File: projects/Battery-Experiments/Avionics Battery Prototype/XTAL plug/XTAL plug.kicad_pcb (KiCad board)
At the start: 2 copper layers, 19.1 x 7.6 mm, 2 parts, among them J1 Conn_01x02, X1 Crystal

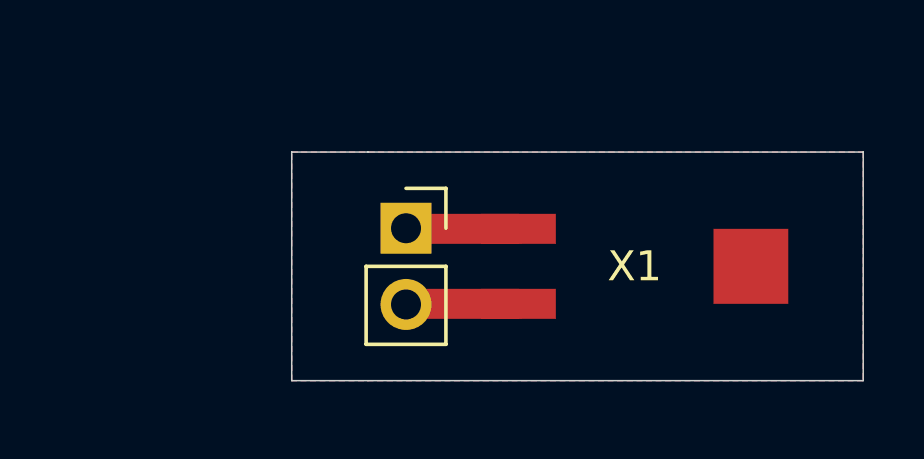
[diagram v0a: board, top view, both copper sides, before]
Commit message: AVB Rev C and XTAL Plug Final
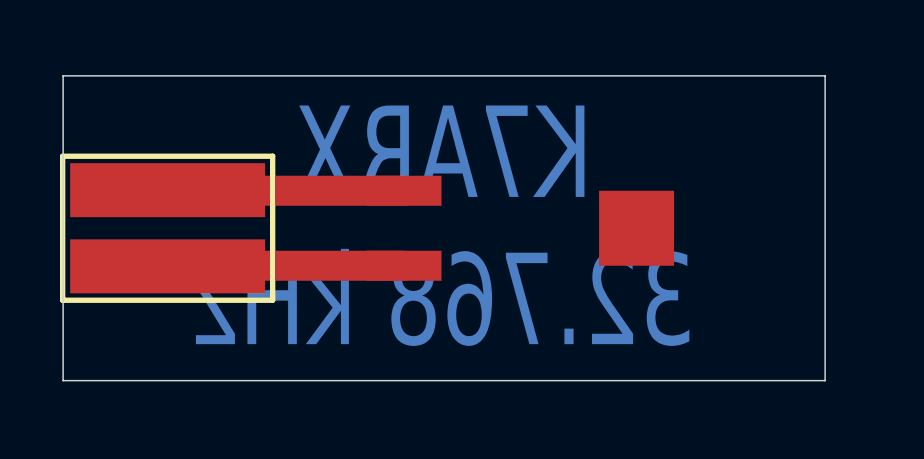
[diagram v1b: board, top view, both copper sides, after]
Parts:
- J1: footprint Connector_PinSocket_2.54mm:PinSocket_1x02_P2.54mm_Vertical -> k7arx:PreciDip 8MM-11 2-pin SMD
- moved J1 4.44 mm to (146.7, 127.0), turned to 270 degrees
- moved X1 4.02 mm to (154.9, 127.0)
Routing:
- net Net-(J1-Pad2): track 3.75 -> 7.86 mm
- net Net-(J1-Pad1): track 3.75 -> 7.86 mm
- removed copper zone on B.Cu, net GND
- removed copper zone on F.Cu, net GND
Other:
- board size 19.1 x 7.6 mm -> 25.4 x 10.2 mm
- board text added: "K7ARX 32.768 kHz"
- board text removed: "K7ARX Crystal Frequency"
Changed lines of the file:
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@@
-(kicad_pcb (version 20171130) (host pcbnew 5.1.9)
+(kicad_pcb (version 20171130) (host pcbnew "(5.1.9)-1")
   (general
     (thickness 1.6)
-    (drawings 8)
-    (tracks 4)
+    (drawings 5)
+    (tracks 2)
     (zones 0)
     (modules 2)
@@
   )
   (layers
-    (0 F.Cu signal hide)
+    (0 F.Cu signal)
     (31 B.Cu signal)
     (32 B.Adhes user)
     (33 F.Adhes user)
     (34 B.Paste user)
-    (35 F.Paste user hide)
+    (35 F.Paste user)
     (36 B.SilkS user)
     (37 F.SilkS user)
     (38 B.Mask user)
-    (39 F.Mask user hide)
+    (39 F.Mask user)
     (40 Dwgs.User user)
     (41 Cmts.User user)
@@
     (pad_to_mask_clearance 0)
     (aux_axis_origin 0 0)
-    (visible_elements FFFFFF7F)
+    (visible_elements 7FFFFFFF)
     (pcbplotparams
       (layerselection 0x010fc_ffffffff)
@@
   )
   (module k7arx:XTAL-CMR200T (layer F.Cu)
-    (at 158.75 128.27 180)
-    (fp_text reference X1 (at 0 0) (layer F.SilkS)
+    (at 154.94 127 180)
+    (fp_text reference X1 (at 0 0) (layer F.SilkS) hide
       (effects (font (size 1 1) (thickness 0.15)))
     )
@@
       (net 1 "Net-(J1-Pad1)"))
   )
-  (module Connector_PinSocket_2.54mm:PinSocket_1x02_P2.54mm_Vertical (layer F.Cu)
-    (at 151.13 127)
-    (descr "Through hole straight socket strip, 1x02, 2.54mm pitch, single row (from Kicad 4.0.7), script generated")
-    (tags "Through hole socket strip THT 1x02 2.54mm single row")
-    (fp_text reference J1 (at 0 -2.77) (layer F.SilkS) hide
+  (module "k7arx:PreciDip 8MM-11 2-pin SMD" (layer F.Cu)
+    (at 146.685 127 270)
+    (fp_text reference J1 (at 0 -1.5 90) (layer F.SilkS) hide
       (effects (font (size 1 1) (thickness 0.15)))
     )
-    (fp_text value Conn_01x02 (at 0 5.31) (layer F.Fab) hide
+    (fp_text value Conn_01x02 (at 0 -3 90) (layer F.Fab) hide
       (effects (font (size 1 1) (thickness 0.15)))
     )
-    (fp_line (start -1.8 4.3) (end -1.8 -1.8) (layer F.CrtYd) (width 0.05))
-    (fp_line (start 1.75 4.3) (end -1.8 4.3) (layer F.CrtYd) (width 0.05))
-    (fp_line (start 1.75 -1.8) (end 1.75 4.3) (layer F.CrtYd) (width 0.05))
-    (fp_line (start -1.8 -1.8) (end 1.75 -1.8) (layer F.CrtYd) (width 0.05))
-    (fp_line (start 0 -1.33) (end 1.33 -1.33) (layer F.SilkS) (width 0.12))
-    (fp_line (start 1.33 -1.33) (end 1.33 0) (layer F.SilkS) (width 0.12))
-    (fp_line (start 1.33 1.27) (end 1.33 3.87) (layer F.SilkS) (width 0.12))
-    (fp_line (start -1.33 3.87) (end 1.33 3.87) (layer F.SilkS) (width 0.12))
-    (fp_line (start -1.33 1.27) (end -1.33 3.87) (layer F.SilkS) (width 0.12))
-    (fp_line (start -1.33 1.27) (end 1.33 1.27) (layer F.SilkS) (width 0.12))
-    (fp_line (start -1.27 3.81) (end -1.27 -1.27) (layer F.Fab) (width 0.1))
-    (fp_line (start 1.27 3.81) (end -1.27 3.81) (layer F.Fab) (width 0.1))
-    (fp_line (start 1.27 -0.635) (end 1.27 3.81) (layer F.Fab) (width 0.1))
-    (fp_line (start 0.635 -1.27) (end 1.27 -0.635) (layer F.Fab) (width 0.1))
-    (fp_line (start -1.27 -1.27) (end 0.635 -1.27) (layer F.Fab) (width 0.1))
-    (fp_text user %R (at 0 1.27 90) (layer F.Fab)
-      (effects (font (size 1 1) (thickness 0.15)))
-    )
-    (pad 1 thru_hole rect (at 0 0) (size 1.7 1.7) (drill 1) (layers *.Cu *.Mask)
+    (fp_line (start 2.4 0) (end -2.4 0) (layer F.SilkS) (width 0.1778))
+    (fp_line (start -2.4 0) (end -2.4 7) (layer F.SilkS) (width 0.1778))
+    (fp_line (start -2.4 7) (end 2.4 7) (layer F.SilkS) (width 0.1778))
+    (fp_line (start 2.4 7) (end 2.4 0) (layer F.SilkS) (width 0.1778))
+    (pad 2 smd rect (at 1.27 3.5 270) (size 1.8 6.5) (layers F.Cu F.Paste F.Mask)
+      (net 2 "Net-(J1-Pad2)"))
+    (pad 1 smd rect (at -1.27 3.5 270) (size 1.8 6.5) (layers F.Cu F.Paste F.Mask)
       (net 1 "Net-(J1-Pad1)"))
-    (pad 2 thru_hole oval (at 0 2.54) (size 1.7 1.7) (drill 1) (layers *.Cu *.Mask)
-      (net 2 "Net-(J1-Pad2)"))
-    (model ${KISYS3DMOD}/Connector_PinSocket_2.54mm.3dshapes/PinSocket_1x02_P2.54mm_Vertical.wrl
-      (at (xyz 0 0 0))
-      (scale (xyz 1 1 1))
-      (rotate (xyz 0 0 0))
-    )
   )
-  (gr_text "K7ARX\nCrystal Frequency" (at 157.48 126.492) (layer B.Mask)
-    (effects (font (size 0.762 0.762) (thickness 0.127)) (justify mirror))
+  (gr_text "K7ARX\n32.768 kHz" (at 152.4 127) (layer B.Cu)
+    (effects (font (size 3.048 2.159) (thickness 0.3556)) (justify mirror))
   )
-  (gr_poly (pts (xy 165.1 131.318) (xy 148.59 131.318) (xy 148.59 128.016) (xy 165.1 128.016)) (layer B.SilkS) (width 0.1))
-  (gr_line (start 149.86 132.08) (end 147.32 132.08) (layer Edge.Cuts) (width 0.05))
-  (gr_line (start 149.86 124.46) (end 147.32 124.46) (layer Edge.Cuts) (width 0.05))
-  (gr_line (start 166.37 124.46) (end 149.86 124.46) (layer Edge.Cuts) (width 0.05))
-  (gr_line (start 166.37 132.08) (end 166.37 124.46) (layer Edge.Cuts) (width 0.05))
-  (gr_line (start 149.86 132.08) (end 166.37 132.08) (layer Edge.Cuts) (width 0.05))
-  (gr_line (start 147.32 124.46) (end 147.32 132.08) (layer Edge.Cuts) (width 0.05))
-  (segment (start 151.15 127.02) (end 151.13 127) (width 1) (layer F.Cu) (net 1))
-  (segment (start 154.875 127.02) (end 151.15 127.02) (width 1) (layer F.Cu) (net 1))
-  (segment (start 151.15 129.52) (end 151.13 129.54) (width 1) (layer F.Cu) (net 2))
-  (segment (start 154.875 129.52) (end 151.15 129.52) (width 1) (layer F.Cu) (net 2))
-  (zone (net 3) (net_name GND) (layer F.Cu) (hatch edge 0.508)
-    (connect_pads (clearance 0.508))
-    (min_thickness 0.254)
-    (fill yes (arc_segments 32) (thermal_gap 0.508) (thermal_bridge_width 0.508))
-    (polygon
-      (pts
-        (xy 166.37 132.08) (xy 147.32 132.08) (xy 147.32 124.46) (xy 166.37 124.46)
-      )
-    )
-  )
-  (zone (net 3) (net_name GND) (layer B.Cu) (hatch edge 0.508)
-    (connect_pads (clearance 0.508))
-    (min_thickness 0.254)
-    (fill yes (arc_segments 32) (thermal_gap 0.508) (thermal_bridge_width 0.508))
-    (polygon
-      (pts
-        (xy 166.37 132.08) (xy 147.32 132.08) (xy 147.32 124.46) (xy 166.37 124.46)
-      )
-    )
-  )
+  (gr_line (start 165.1 121.92) (end 139.7 121.92) (layer Edge.Cuts) (width 0.05))
+  (gr_line (start 165.1 132.08) (end 165.1 121.92) (layer Edge.Cuts) (width 0.05))
+  (gr_line (start 139.7 132.08) (end 165.1 132.08) (layer Edge.Cuts) (width 0.05))
+  (gr_line (start 139.7 121.92) (end 139.7 132.08) (layer Edge.Cuts) (width 0.05))
+  (segment (start 151.065 125.75) (end 143.205 125.75) (width 1) (layer F.Cu) (net 1))
+  (segment (start 151.065 128.25) (end 143.205 128.25) (width 1) (layer F.Cu) (net 2))
 )
